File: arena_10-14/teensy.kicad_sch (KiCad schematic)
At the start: 46 parts, among them J1 Cetus RJ45 Magjack, J2 Qwiic, J3 Conn_01x02, J4 Conn_01x02, J5 Conn_Coaxial, J6 Conn_Coaxial, U1 Teensy4.1, U2 SN74LVC1T45DBV, U3 SN74LVC1T45DBV

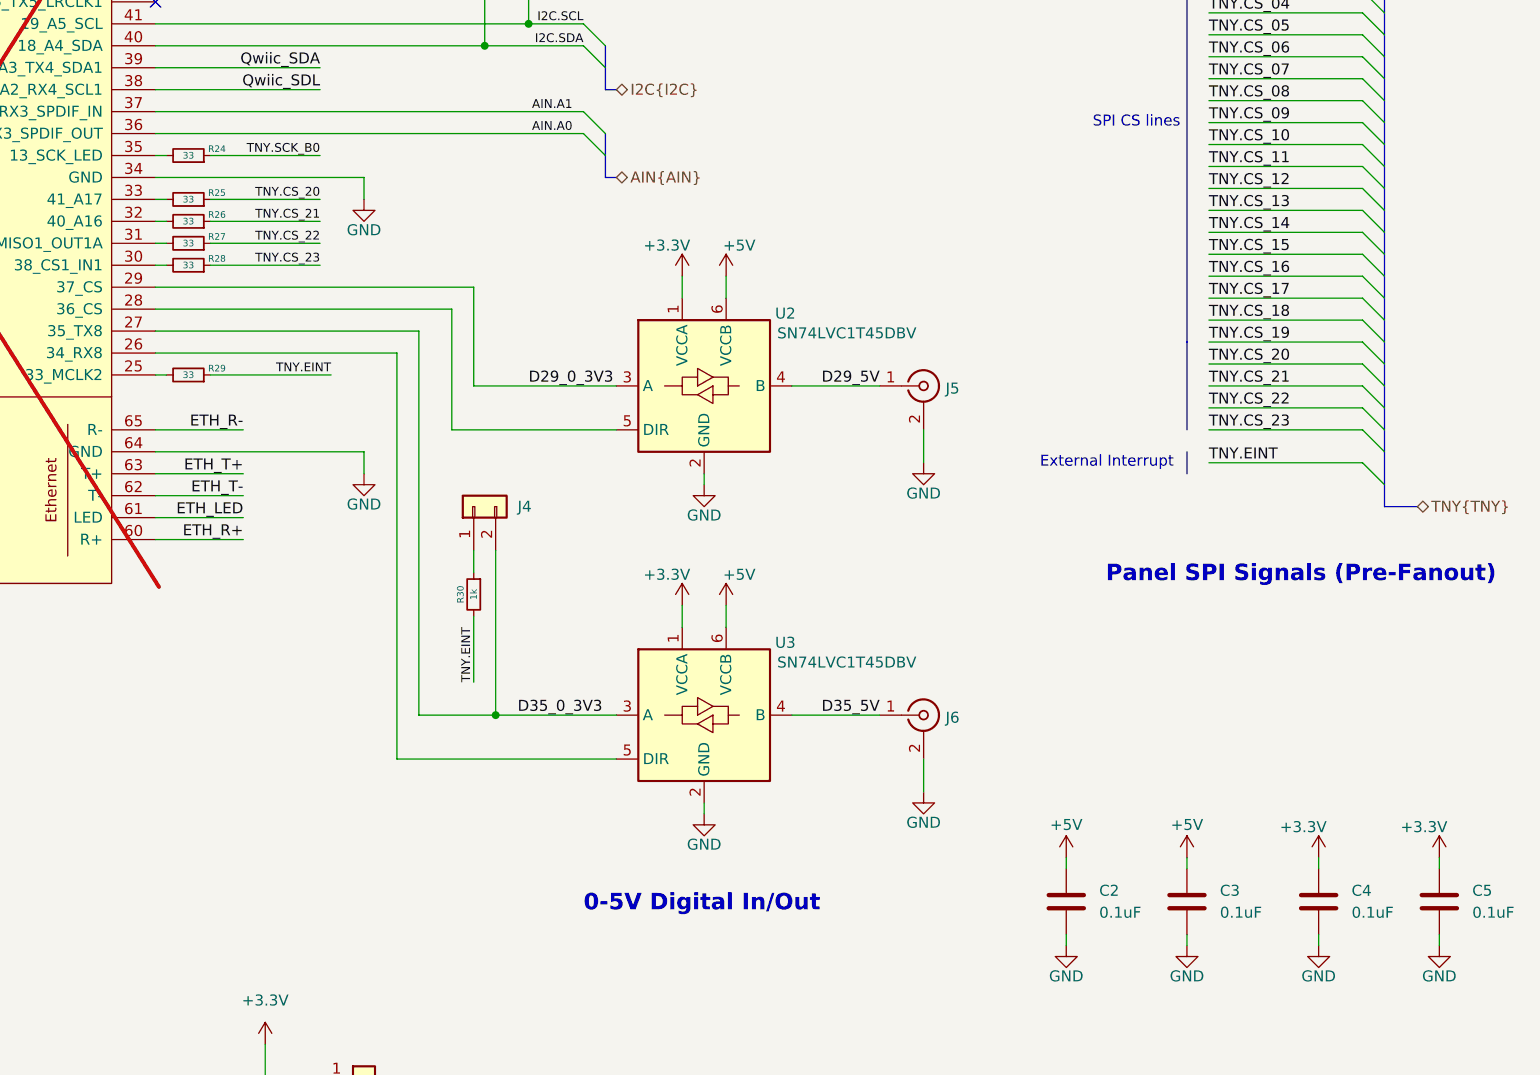
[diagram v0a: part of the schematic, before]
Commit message: feat: reduce 10-14 arena to 10 panel columns and add digital IO channels
Schematic
- Remove panel columns P11 and P12; the Panels sheet now holds P1..P10.
- Re-split the SPI banks for 10 panels: B0 serves P1-P5, B1 serves
  P6-P10 (CIPO enables, SCK/COPI/EINT fan-out).
- Re-pair the chip selects: CS_00..19 each fan out to (Pn, Pn+5), and
  the CS_20..23 fan-out sheets are gone.
- The shared SCK/COPI/EINT dual buffers now drive P1/P2, P3/P4, P6/P7
  and P8/P9. The buffers for P5 and P10 each drive a single panel.
- Move the Teensy digital IO channel (SN74LVC1T45 level shifter and BNC
  connector) into a new DIO.kicad_sch sub-sheet and instance it four
  times (Digital IO 01..04).

PCB
- Update from the schematic: the P11/P12 columns and their parts are
  removed (623 -> 547 footprints, no P11/P12 nets left). The freed
  references U78-U80, J25, J26 and J34 now belong to the digital IO
  channels.
- Most of the old 12-panel routing is removed (4471 -> 1393
  tracks/vias).

Placement scripts (assets/placement/)
- 01, 02: end each footprint block at its own closing paren. The last
  footprint in the file used to extend to the end of the file, so 02
  added an angle to every via and KiCad refused to open the board
  ("Expecting ')'").
- 03: replicate to P1..P10 only and ignore CIPO-enable sheets beyond
  P10. Read the B0/B1 bank of the PAN and TNY nets from the board
  instead of hardcoding P1-P6 / P7-P12. Same footprint-block fix.
- 05: read each CS group's panel pair and midpoint anchor from the
  fan-out sheet names instead of hardcoding P(4+j), and stop if a
  midpoint is not a populated connector. Same footprint-block fix (05
  rewrites footprints, so it could corrupt vias the same way 02 did).

Known gaps, to follow up
- 05 stops on the new CS pairing: the P1/P6 midpoint is P3.5, so an
  anchor for each group still has to be chosen.
- 02 and 03 still pair the shared buffers as P1/P2, P3/P4, P5/P6,
  P7/P8, P9/P10, anchored on the even connector. With the new B1
  p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
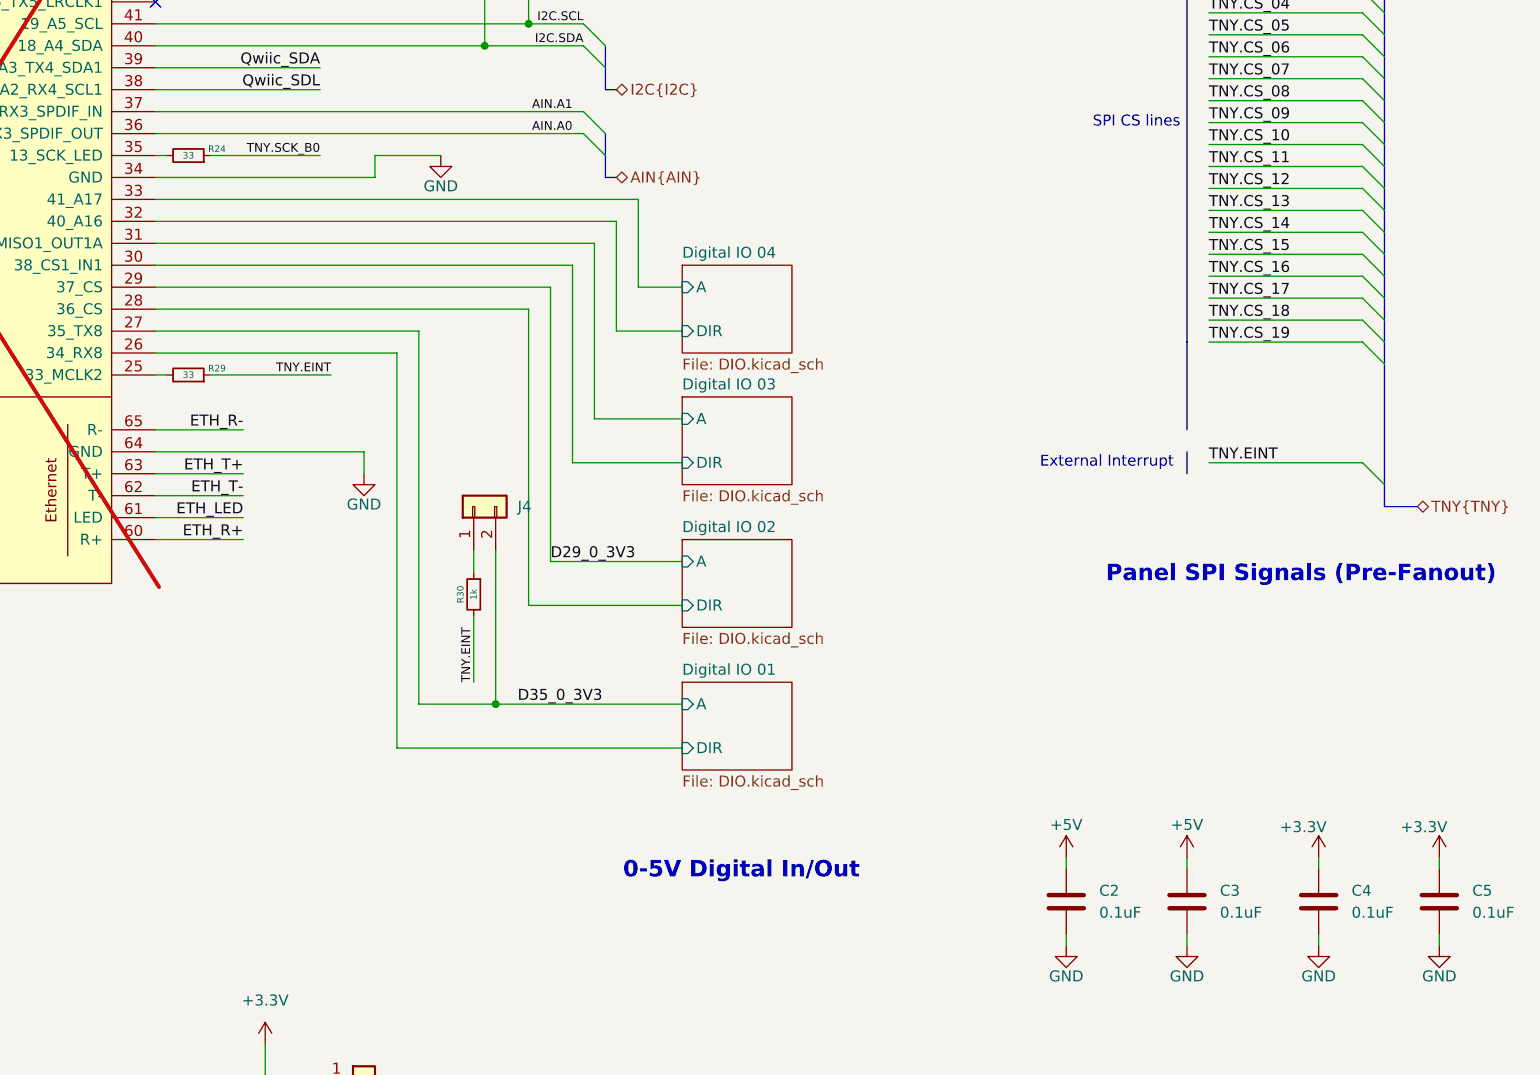
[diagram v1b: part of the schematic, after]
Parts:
- removed J5, J6: Conn_Coaxial, BNC:BNC, symbol Connector:Conn_Coaxial
- removed R25, R26, R27, R28: 33, Resistor_SMD:R_0402_1005Metric, symbol Device:R_Small
- removed U2, U3: SN74LVC1T45DBV, Package_TO_SOT_SMD:SOT-23-6, symbol Logic_LevelTranslator:SN74LVC1T45DBV
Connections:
- net Digital IO 04/DIR: now reaches U1.32 (40_A16)
- net Digital IO 01/DIR: now reaches U1.26 (34_RX8)
- net Digital IO 03/DIR: now reaches U1.30 (38_CS1_IN1)
- net Digital IO 02/DIR: now reaches U1.28 (36_CS)
- net Digital IO 03/A: now reaches U1.31 (39_MISO1_OUT1A)
- net Digital IO 04/A: now reaches U1.33 (41_A17)
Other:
- added sheet Digital IO 01 (DIO.kicad_sch)
- added sheet Digital IO 02 (DIO.kicad_sch)
- added sheet Digital IO 03 (DIO.kicad_sch)
- added sheet Digital IO 04 (DIO.kicad_sch)

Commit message: first draft
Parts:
- removed C2, C3, C4, C5: 0.1uF, Capacitor_SMD:C_0402_1005Metric, symbol Device:C

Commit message: first moat
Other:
- sheet Digital IO 01 renamed DIO2
- sheet Digital IO 02 renamed DIO1
- sheet Digital IO 03 renamed DIO4
- sheet Digital IO 04 renamed DIO3
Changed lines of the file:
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@@
 			(color 0 0 0 0)
 		)
-		(property "Sheetname" "Digital IO 04"
+		(property "Sheetname" "DIO3"
 			(at 166.37 83.1084 0)
 			(show_name no)
@@
 			(color 0 0 0 0)
 		)
-		(property "Sheetname" "Digital IO 01"
+		(property "Sheetname" "DIO2"
 			(at 166.37 131.3684 0)
 			(show_name no)
@@
 			(color 0 0 0 0)
 		)
-		(property "Sheetname" "Digital IO 02"
+		(property "Sheetname" "DIO1"
 			(at 166.37 114.8584 0)
 			(show_name no)
@@
 			(color 0 0 0 0)
 		)
-		(property "Sheetname" "Digital IO 03"
+		(property "Sheetname" "DIO4"
 			(at 166.37 98.3484 0)
 			(show_name no)

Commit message: better 15V GND
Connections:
- net Qwiic_SDL renamed Qwiic_SCL
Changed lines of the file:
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@@
 	(title_block
 		(title "G6 Teensy 10-14 Arena")
-		(date "2026-08-03")
+		(date "2026-10-25")
 		(rev "v1.0")
 		(company "Reiser Lab @ Janelia | HHMI")
@@
 		)
 	)
-	(label "Qwiic_SDL"
+	(label "Qwiic_SCL"
 		(at 124.46 63.5 180)
 		(effects
@@
 		)
 	)
-	(label "Qwiic_SDL"
+	(label "Qwiic_SCL"
 		(at 113.03 185.42 0)
 		(effects
@@
 			)
 		)
-		(property "Description" ""
+		(property "Description" "Generic connector, single row, 01x04, script generated (kicad-library-utils/schlib/autogen/connector/)"
 			(at 129.54 180.34 0)
 			(hide yes)

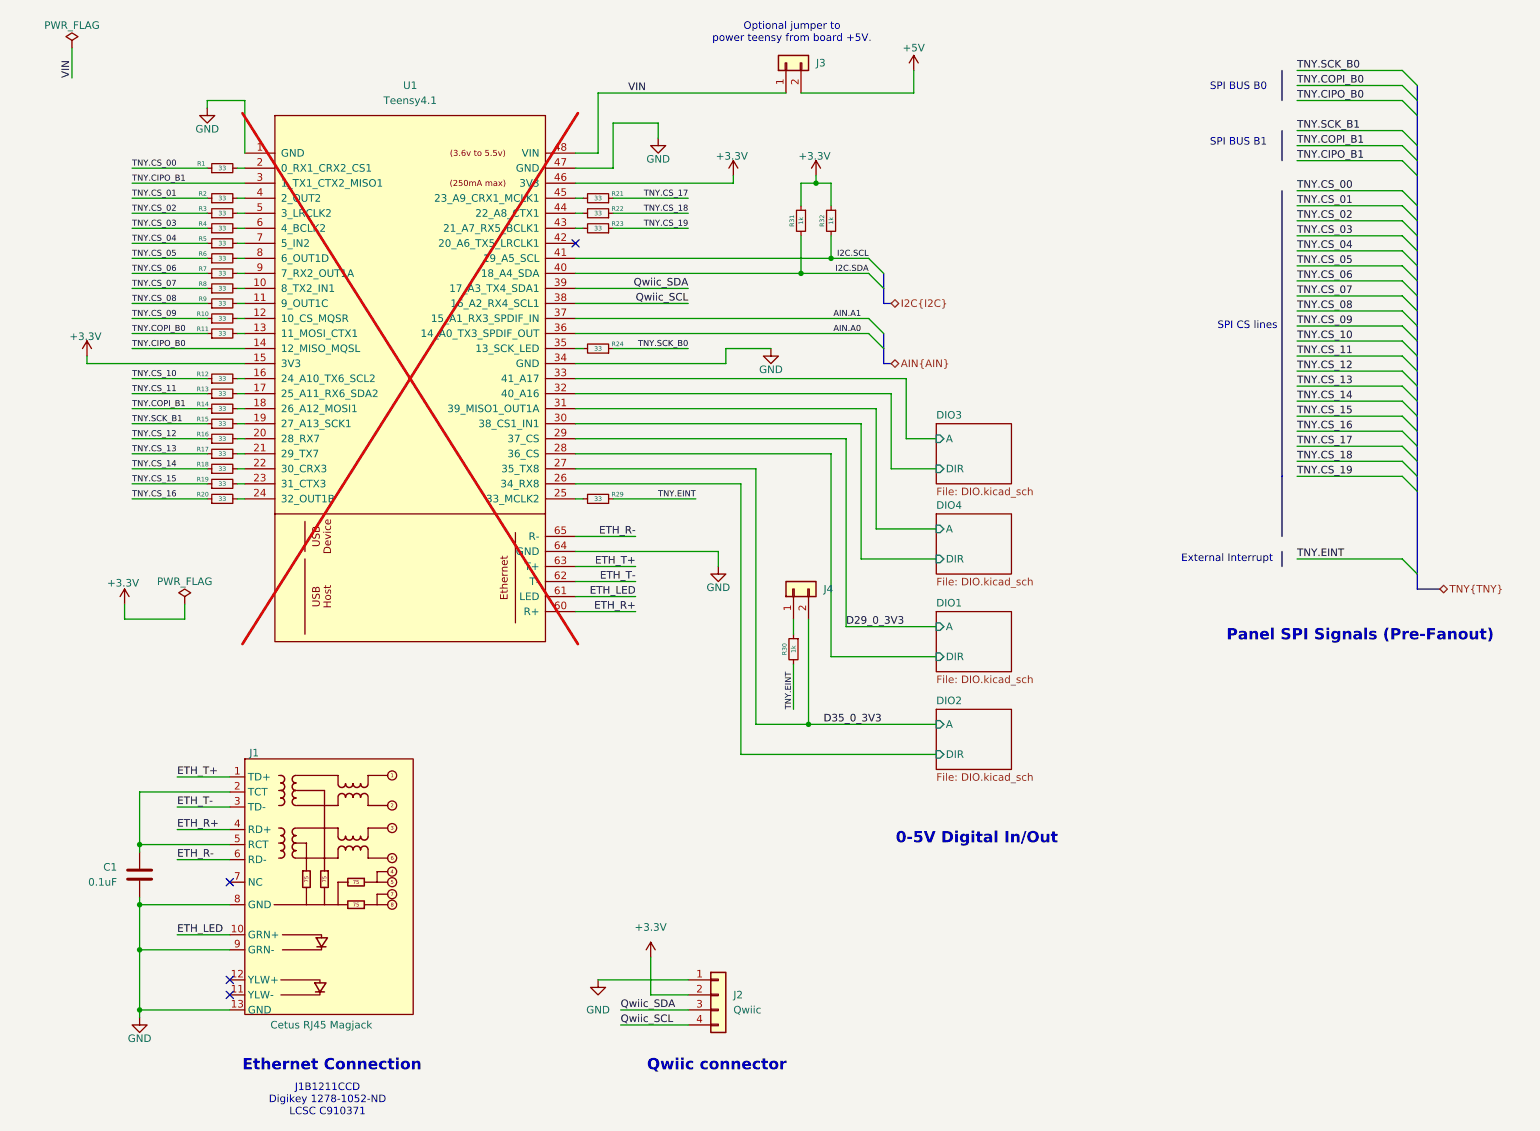
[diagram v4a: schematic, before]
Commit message: Link DIO 3 & 4 DIR, place connectors
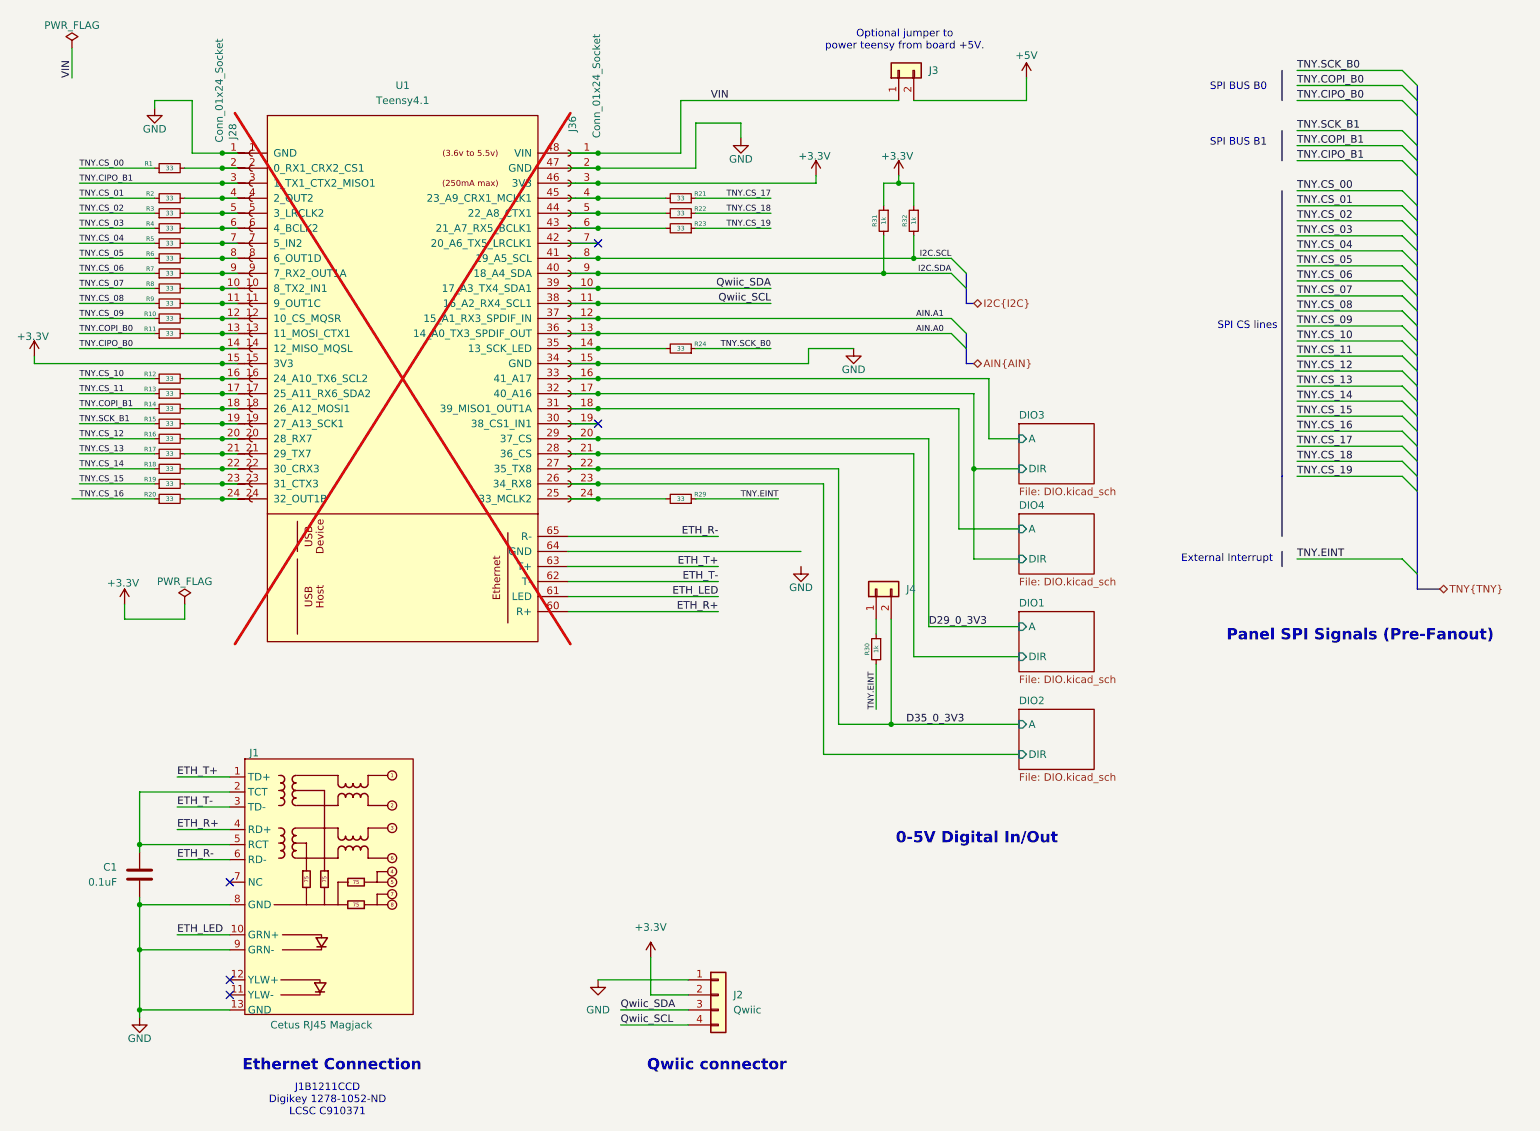
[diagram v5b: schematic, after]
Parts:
- added J28, J36: Conn_01x24_Socket, PinSocket_1x24_P2.54mm_Vertical, symbol Connector:Conn_01x24_Socket
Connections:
- net +3.3V: now also J28.15 (Pin_15), J36.3 (Pin_3)
- net AIN.A0: now also J36.13 (Pin_13)
- net AIN.A1: now also J36.12 (Pin_12)
- net D29_0_3V3: now also J36.20 (Pin_20)
- net D35_0_3V3: now also J36.22 (Pin_22)
- net DIO1/DIR: now also J36.21 (Pin_21)
- net DIO2/DIR: now also J36.23 (Pin_23)
- net DIO3/A: now also J36.16 (Pin_16)
- net DIO3/DIR: now also J36.17 (Pin_17)
- net DIO4/A: now also J36.18 (Pin_18)
- net GND: now also J28.1 (Pin_1), J36.15 (Pin_15), J36.2 (Pin_2); no longer U1.64 (GND)
- net I2C.SCL: now also J36.8 (Pin_8)
- net I2C.SDA: now also J36.9 (Pin_9)
- net Qwiic_SCL: now also J36.11 (Pin_11)
- net Qwiic_SDA: now also J36.10 (Pin_10)
- net TNY.CIPO_B0: now also J28.14 (Pin_14)
- net TNY.CIPO_B1: now also J28.3 (Pin_3)
- net VIN: now also J36.1 (Pin_1)
- net at R21.2, U1.45 (23_A9_CRX1_MCLK1): now also J36.4 (Pin_4)
- net at R2.2, U1.4 (2_OUT2): now also J28.4 (Pin_4)
- net at R3.2, U1.5 (3_LRCLK2): now also J28.5 (Pin_5)
- net at R10.2, U1.12 (10_CS_MQSR): now also J28.12 (Pin_12)
- net at R19.2, U1.23 (31_CTX3): now also J28.23 (Pin_23)
- net at R23.2, U1.43 (21_A7_RX5_BCLK1): now also J36.6 (Pin_6)
- net at R22.2, U1.44 (22_A8_CTX1): now also J36.5 (Pin_5)
- net at R16.2, U1.20 (28_RX7): now also J28.20 (Pin_20)
- net at R8.2, U1.10 (8_TX2_IN1): now also J28.10 (Pin_10)
- net at R6.2, U1.8 (6_OUT1D): now also J28.8 (Pin_8)
- net at R24.2, U1.35 (13_SCK_LED): now also J36.14 (Pin_14)
- net at R14.2, U1.18 (26_A12_MOSI1): now also J28.18 (Pin_18)
- net at R11.2, U1.13 (11_MOSI_CTX1): now also J28.13 (Pin_13)
- net at R4.2, U1.6 (4_BCLK2): now also J28.6 (Pin_6)
- net at R15.2, U1.19 (27_A13_SCK1): now also J28.19 (Pin_19)
- net at R7.2, U1.9 (7_RX2_OUT1A): now also J28.9 (Pin_9)
- net at R29.2, U1.25 (33_MCLK2): now also J36.24 (Pin_24)
- net at R18.2, U1.22 (30_CRX3): now also J28.22 (Pin_22)
- net at R12.2, U1.16 (24_A10_TX6_SCL2): now also J28.16 (Pin_16)
- net at R9.2, U1.11 (9_OUT1C): now also J28.11 (Pin_11)
- net at R13.2, U1.17 (25_A11_RX6_SDA2): now also J28.17 (Pin_17)
- net at R1.2, U1.2 (0_RX1_CRX2_CS1): now also J28.2 (Pin_2)
- net at R17.2, U1.21 (29_TX7): now also J28.21 (Pin_21)
- net at R20.2, U1.24 (32_OUT1B): now also J28.24 (Pin_24)
- net at U1.42 (20_A6_TX5_LRCLK1): now also J36.7 (Pin_7)
- net at R5.2, U1.7 (5_IN2): now also J28.7 (Pin_7)
- net DIO4/DIR: no longer names the net of U1.30 (38_CS1_IN1)
- net DIO4/DIR: now also J36.19 (Pin_19)
- no-connect marks 4 -> 5
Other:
- moved on the sheet: J3, J4, R1, R10, R11, R12, R13, R14, R15, R16, R17, R18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
